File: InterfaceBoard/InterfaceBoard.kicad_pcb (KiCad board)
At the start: 4 copper layers, 100 x 86 mm, 137 parts, among them J1 Conn_ARM_JTAG_SWD_10, J2 USB_B, J3 Keithley_50-Pin_Connector, J4 DB9_Female_MountingHoles, P1 RB1-125BAG1A, Q1 BC848W, Q2 BC848W, Q3 BC848W, U1 W5500, U2 FT231XQ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

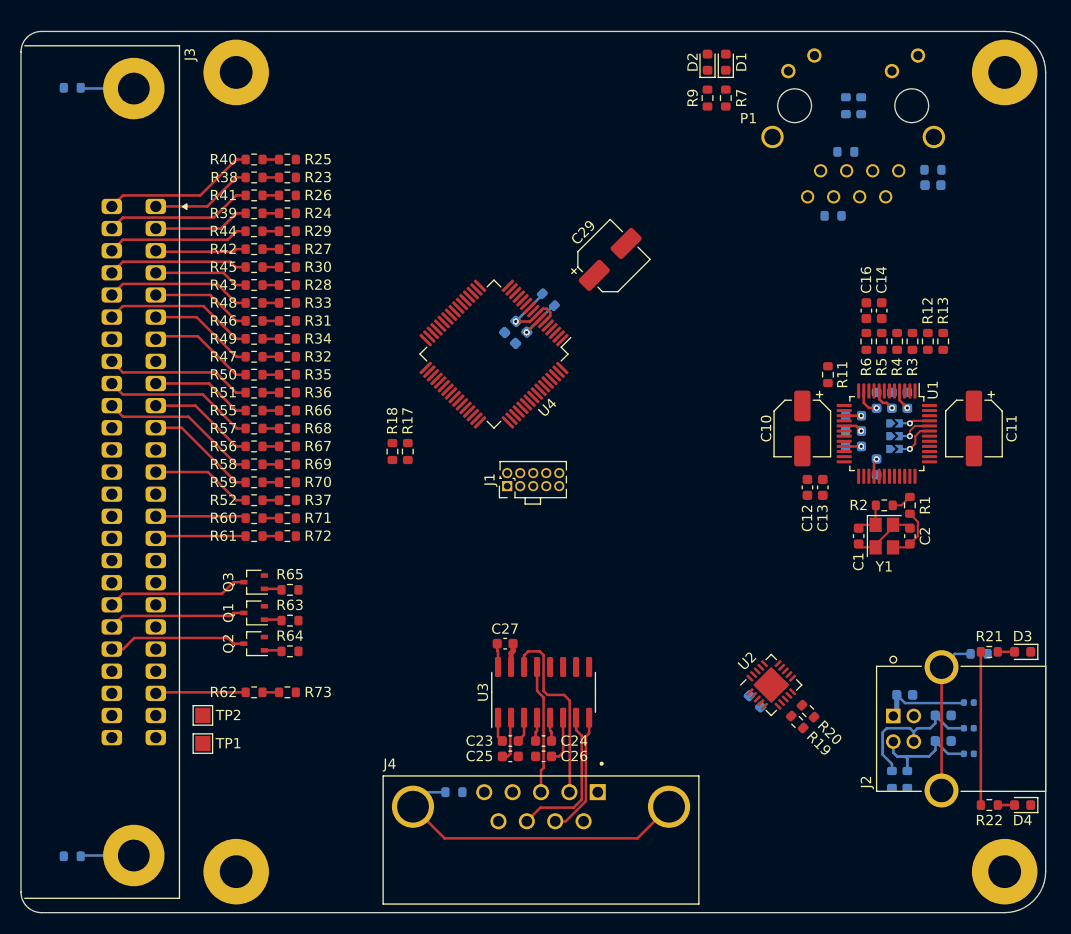
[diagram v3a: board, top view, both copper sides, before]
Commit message: InterfaceBoard: Update connector footprint
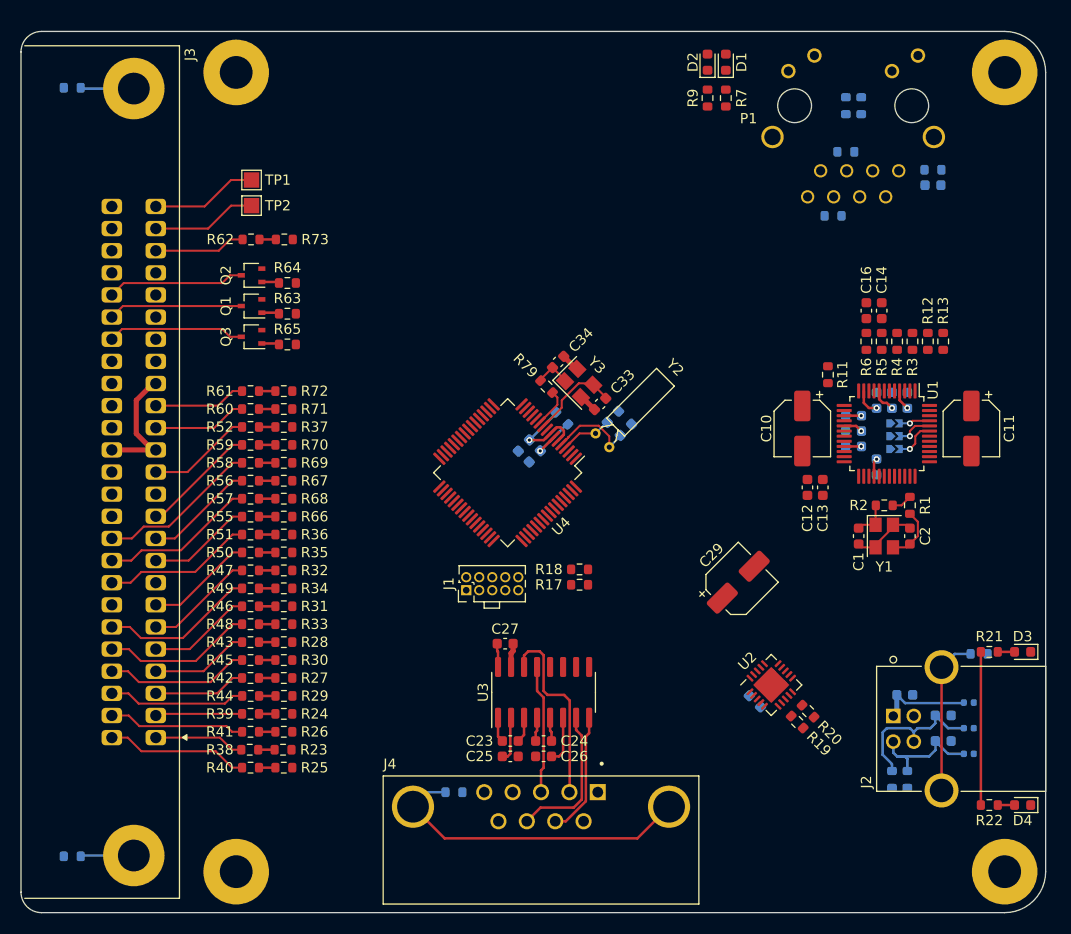
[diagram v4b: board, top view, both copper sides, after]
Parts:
- added C31: 22pF, Capacitor_SMD:C_0603_1608Metric, B.Cu at (97.8, 66.6)
- added C32: 22pF, Capacitor_SMD:C_0603_1608Metric, B.Cu at (99.0, 67.9)
- added C33: 12pF, Capacitor_SMD:C_0603_1608Metric, F.Cu at (96.5, 65.4)
- added C34: 12pF, Capacitor_SMD:C_0603_1608Metric, F.Cu at (92.4, 61.3)
- added R79: 1.6k, Resistor_SMD:R_0603_1608Metric, F.Cu at (91.3, 63.7)
- added Y2: 32.768 kHz, Crystal:Crystal_C26-LF_D2.1mm_L6.5mm_Horizontal, F.Cu at (97.4, 69.6)
- added Y3: 24 MHz, Crystal:Crystal_SMD_3225-4Pin_3.2x2.5mm, F.Cu at (94.5, 63.3)
- moved R25 59.4 mm to (65.7, 100.8)
- moved R40 59.4 mm to (62.4, 100.8)
- moved R23 55.9 mm to (65.6, 99.1)
- moved R38 55.9 mm to (62.3, 99.1)
- moved TP1 55.2 mm to (62.5, 43.5), turned to 90 degrees
- moved R26 52.4 mm to (65.7, 97.3)
- moved R41 52.4 mm to (62.4, 97.3)
- moved TP2 50.0 mm to (62.5, 46.0), turned to 90 degrees
- moved R24 48.9 mm to (65.7, 95.6)
- moved R39 48.9 mm to (62.4, 95.6)
- moved R29 45.4 mm to (65.7, 93.8)
- moved R44 45.4 mm to (62.4, 93.8)
- moved R62 44.2 mm to (62.5, 49.3)
- moved R73 44.2 mm to (65.7, 49.3)
- moved R27 41.9 mm to (65.7, 92.1)
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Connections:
- net /USB/USB_PULLUP renamed /MCU/USB_PULLUP
- J1 pad 1: unconnected-(J1-Pad1) -> +3V3
- U4 pad 10: unconnected-(U4-Pad10) -> Net-(C33-Pad1)
- U4 pad 11: unconnected-(U4-Pad11) -> Net-(R79-Pad2)
- U4 pad 13: unconnected-(U4-Pad13) -> /Print_Cmd
- U4 pad 14: unconnected-(U4-Pad14) -> /Trigger
- U4 pad 15: /Data_4e0 -> /Hold2
- U4 pad 16: /Data_1e0 -> /Hold1
- U4 pad 19: unconnected-(U4-Pad19) -> /Sensitivity_1e0
- U4 pad 22: unconnected-(U4-Pad22) -> /Polarity
- U4 pad 24: unconnected-(U4-Pad24) -> /Range_1e1
- U4 pad 25: /Data_8e0 -> /Range_8e0
- U4 pad 26: /Data_2e0 -> /Range_2e0
- U4 pad 27: /Data_4e1 -> /Range_4e0
- U4 pad 28: /Data_1e1 -> /Range_1e0
- U4 pad 29: /Data_8e1 -> /Overload
- U4 pad 3: unconnected-(U4-Pad3) -> /Sensitivity_2e0
- U4 pad 30: /Data_2e1 -> /Data_1e3
- U4 pad 31: /Data_4e2 -> /Data_2e2
- U4 pad 32: /Data_1e2 -> /Data_8e2
- U4 pad 33: /Data_8e2 -> /Data_1e2
- U4 pad 34: /Data_2e2 -> /Data_4e2
- U4 pad 35: /Data_1e3 -> /Data_2e1
- U4 pad 36: /Overload -> /Data_8e1
- U4 pad 37: /Range_1e0 -> /Data_1e1
- U4 pad 38: /Range_4e0 -> /Data_4e1
- U4 pad 39: /Range_2e0 -> /Data_2e0
- U4 pad 4: unconnected-(U4-Pad4) -> Net-(C31-Pad1)
- U4 pad 40: /Range_8e0 -> /Data_8e0
- U4 pad 41: /Range_1e1 -> /Data_1e0
- U4 pad 42: /Polarity -> /Data_4e0
- U4 pad 47: /Sensitivity_1e0 -> unconnected-(U4-Pad47)
- U4 pad 48: /Sensitivity_2e0 -> unconnected-(U4-Pad48)
- U4 pad 49: /Hold1 -> unconnected-(U4-Pad49)
- U4 pad 5: unconnected-(U4-Pad5) -> Net-(C32-Pad1)
- U4 pad 50: /Hold2 -> unconnected-(U4-Pad50)
- U4 pad 51: /Trigger -> unconnected-(U4-Pad51)
- U4 pad 52: /Print_Cmd -> unconnected-(U4-Pad52)
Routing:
- net +15V: track 0.00 -> 12.7 mm
- net /50pin/Ref_Hi: track 0.00 -> 10.4 mm
- net /50pin/Ref_Lo: track 0.00 -> 10.3 mm
- net Net-(C33-Pad1): track 0.00 -> 8.92 mm
- net Net-(C32-Pad1): track 0.00 -> 8.51 mm
- net Net-(C31-Pad1): track 0.00 -> 5.16 mm
- net Net-(R79-Pad2): track 0.00 -> 3.84 mm
- net GND: track 8.83 -> 12.5 mm
- net Net-(C34-Pad1): track 0.00 -> 3.59 mm
- net Net-(J3-Pad1): track 9.94 -> 8.83 mm
- net Net-(J3-Pad27): track 14.4 -> 13.4 mm
- net Net-(J3-Pad26): track 15.0 -> 13.9 mm
- net Net-(J3-Pad2): track 9.39 -> 8.49 mm

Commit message: InterfaceBoard: Add 3.3 V regulater, test points.
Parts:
- added C35: 10 uF, Capacitor_SMD:C_0805_2012Metric, F.Cu at (86.2, 41.5)
- added C36: 100 nF, Capacitor_SMD:C_0603_1608Metric, F.Cu at (91.8, 43.5)
- added C37: 10 uF, Capacitor_SMD:C_0805_2012Metric, F.Cu at (84.2, 41.5)
- added C38: 22 uF, Capacitor_SMD:C_0805_2012Metric, F.Cu at (86.2, 45.0)
- added C39: 22 uF, Capacitor_SMD:C_0805_2012Metric, F.Cu at (84.2, 45.0)
- added FB1: 1k, Inductor_SMD:L_0805_2012Metric, F.Cu at (118.5, 70.8)
- added J5: SPI, Connector_PinHeader_1.27mm:PinHeader_1x06_P1.27mm_Vertical, F.Cu at (109.5, 105.9)
- added J6: RS232, Connector_PinHeader_1.27mm:PinHeader_1x05_P1.27mm_Vertical, F.Cu at (98.5, 96.1)
- added J7: UART, Connector_PinHeader_1.27mm:PinHeader_1x05_P1.27mm_Vertical, F.Cu at (116.8, 107.2)
- added L1: 2.2 uH, Inductor_SMD:L_Taiyo-Yuden_NR-50xx, F.Cu at (90.2, 47.0)
- added R80: 0, Resistor_SMD:R_0603_1608Metric, F.Cu at (80.0, 31.2)
- added R81: 0, Resistor_SMD:R_0603_1608Metric, F.Cu at (80.0, 32.8)
- added R82: 0, Resistor_SMD:R_0603_1608Metric, F.Cu at (80.0, 34.2)
- added R83: 31.6k, Resistor_SMD:R_0603_1608Metric, F.Cu at (91.8, 42.0)
- added R84: 10k, Resistor_SMD:R_0603_1608Metric, F.Cu at (91.8, 40.5)
- added TP3: V_In, TestPoint:TestPoint_THTPad_1.5x1.5mm_Drill0.7mm, F.Cu at (88.0, 32.8)
- added TP4: V_Switch, TestPoint:TestPoint_THTPad_1.5x1.5mm_Drill0.7mm, F.Cu at (94.8, 47.0)
- added TP5: V_3.3, TestPoint:TestPoint_THTPad_1.5x1.5mm_Drill0.7mm, F.Cu at (98.5, 42.2)
- added TP6: V_EXT, TestPoint:TestPoint_THTPad_2.0x2.0mm_Drill1.0mm, F.Cu at (72.5, 32.0)
- added TP7: GND, TestPoint:TestPoint_THTPad_2.0x2.0mm_Drill1.0mm, F.Cu at (68.5, 32.0)
- added U5: AP62250Z6, Package_TO_SOT_SMD:SOT-563, F.Cu at (88.8, 43.0)
- C10, C11: footprint Capacitor_SMD:CP_Elec_5x5.9 -> Capacitor_SMD:C_0805_2012Metric
- J1: value Conn_ARM_JTAG_SWD_10 -> SWD
- moved C11 13.2 mm to (120.5, 72.8)
- moved C29 10.9 mm to (101.2, 76.2)
- moved R11 7.59 mm to (121.0, 55.2), turned to 90 degrees
- moved C12 7.57 mm to (117.7, 66.0), turned to 180 degrees
- moved C13 6.02 mm to (117.7, 67.5), turned to 180 degrees
- moved C10 4.19 mm to (117.5, 63.8), turned to 180 degrees
- moved C14 4.00 mm to (124.0, 52.2)
- moved C16 4.00 mm to (122.5, 52.2)
- moved R12 4.00 mm to (128.5, 55.2)
- moved R13 4.00 mm to (130.0, 55.2)
- moved R3 4.00 mm to (127.0, 55.2)
- moved R4 4.00 mm to (125.5, 55.3)
- moved R5 4.00 mm to (124.0, 55.2)
- moved R6 4.00 mm to (122.5, 55.2)
- moved C1 2.85 mm to (122.5, 75.5)
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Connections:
- net /USB/V_USB renamed /Power Supply/V_USB
- C10 pad 1: +3V3 -> /Ethernet Interface/W5500_AVDD
- C3 pad 2: +3V3 -> /Ethernet Interface/W5500_AVDD
- C4 pad 2: +3V3 -> /Ethernet Interface/W5500_AVDD
- C5 pad 2: +3V3 -> /Ethernet Interface/W5500_AVDD
- C6 pad 2: +3V3 -> /Ethernet Interface/W5500_AVDD
- C7 pad 2: +3V3 -> /Ethernet Interface/W5500_AVDD
- C9 pad 2: +3V3 -> /Ethernet Interface/W5500_AVDD
- U1 pad 11: +3V3 -> /Ethernet Interface/W5500_AVDD
- U1 pad 15: +3V3 -> /Ethernet Interface/W5500_AVDD
- U1 pad 17: +3V3 -> /Ethernet Interface/W5500_AVDD
- U1 pad 21: +3V3 -> /Ethernet Interface/W5500_AVDD
- U1 pad 4: +3V3 -> /Ethernet Interface/W5500_AVDD
- U1 pad 8: +3V3 -> /Ethernet Interface/W5500_AVDD
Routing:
- net /Ethernet Interface/W5500_AVDD: track 0.00 -> 26.6 mm, vias 0 -> 6
- net /Power Supply/V_IN: track 0.00 -> 8.17 mm
- net /Power Supply/SW_Inductor: track 0.00 -> 6.26 mm
- net Net-(R6-Pad1): track 0.00 -> 6.19 mm
- net Net-(R11-Pad1): track 0.00 -> 5.99 mm
- net /Ethernet Interface/ETH_PORT_TX+: track 0.00 -> 5.86 mm
- net Net-(R5-Pad1): track 0.00 -> 5.78 mm
- net Net-(R4-Pad1): track 0.00 -> 5.78 mm
- net Net-(R3-Pad1): track 0.00 -> 5.37 mm
- net Net-(R1-Pad2): track 2.02 -> 5.30 mm
- net Net-(R83-Pad2): track 0.00 -> 3.13 mm
- net Net-(C1-Pad2): track 3.69 -> 6.56 mm
- net +3V3: track 23.0 -> 25.2 mm, vias 8 -> 4
- net Net-(C13-Pad1): track 0.00 -> 1.92 mm
- net Net-(C12-Pad1): track 0.00 -> 1.92 mm
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- added copper zone on F.Cu, net +3V3
- added copper zone on F.Cu, net /Power Supply/SW_Inductor
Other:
- board text added: "+15V"
- board text added: "3.3 V Regulator"
- board text added: "3V3"
- board text added: "CS"
- board text added: "CTS"
- board text added: "EXT"
- board text added: "GND"
- board text added: "PICO"
- board text added: "POCI"
- board text added: "RTS"
- board text added: "RX"
- board text added: "SCK"
- board text added: "TX"
- board text added: "USB"

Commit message: InterfaceBoard: MAX232 -> MAX3232
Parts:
- C23, C24, C25, C26: value 1uF -> 100nF
- U3: value MAX232 -> MAX3232
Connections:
- C27 pad 1: +5V -> +3V3
- U3 pad 16: +5V -> +3V3
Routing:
- net +5V: track 2.31 -> 0.00 mm
- net +3V3: track 25.2 -> 27.5 mm

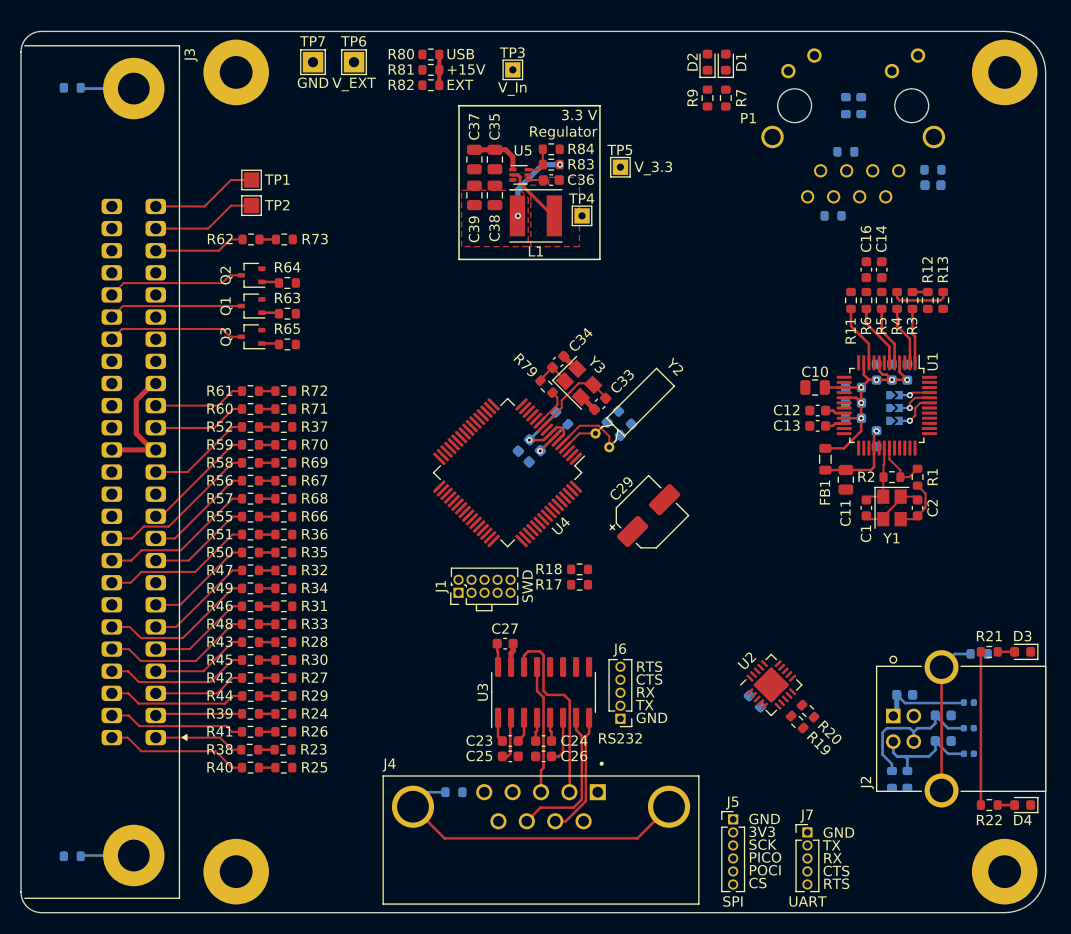
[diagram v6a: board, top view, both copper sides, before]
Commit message: InterfaceBoard: Routed Ethernet
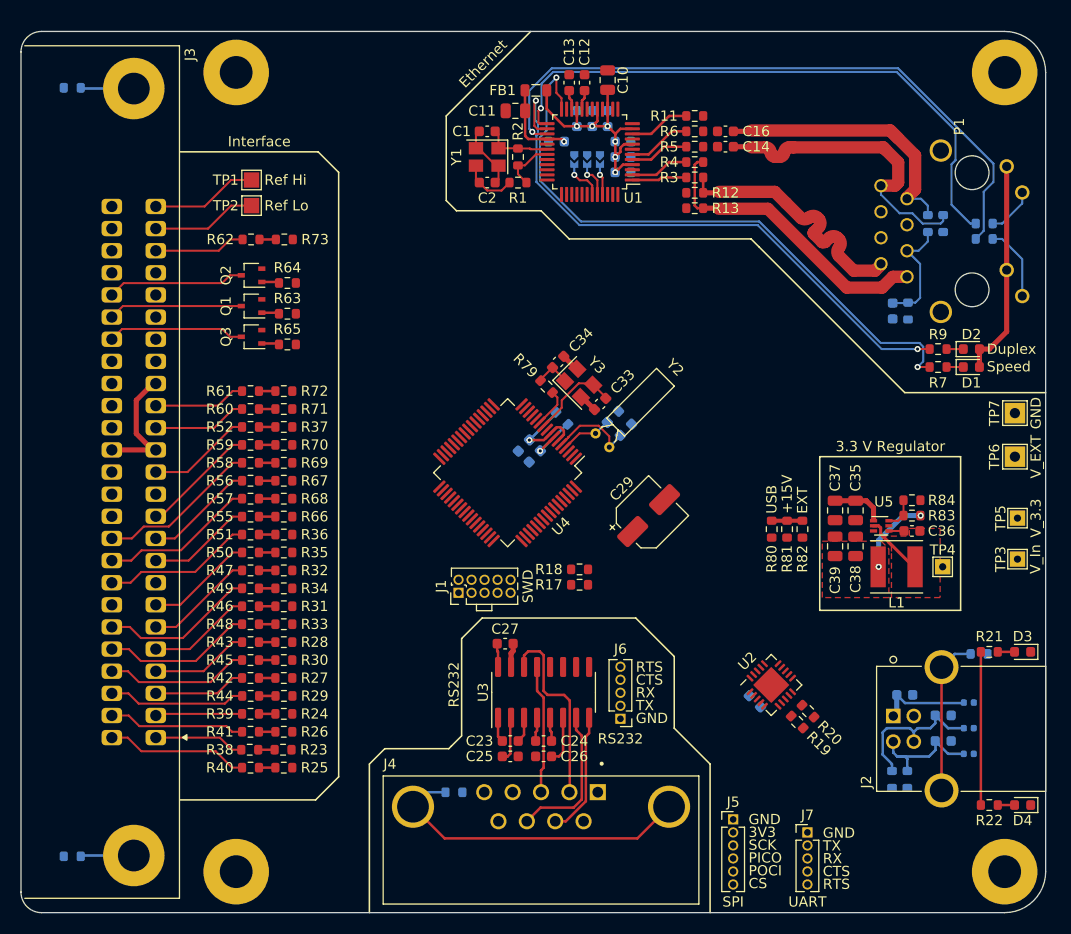
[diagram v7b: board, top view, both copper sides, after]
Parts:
- moved TP7 76.6 mm to (137.0, 66.2), turned to 90 degrees
- moved TP6 75.1 mm to (137.0, 70.5), turned to 90 degrees
- moved TP3 68.6 mm to (137.2, 80.5), turned to 90 degrees
- moved R80 57.0 mm to (113.3, 77.6), turned to 90 degrees
- moved R81 56.7 mm to (114.8, 77.6), turned to 90 degrees
- moved R82 56.5 mm to (116.3, 77.6), turned to 90 degrees
- moved C2 52.7 mm to (85.5, 43.8), turned to 180 degrees
- moved Y1 52.3 mm to (85.5, 41.2), turned to 180 degrees
- moved C1 52.1 mm to (85.5, 38.8), turned to 0 degrees
- moved TP5 51.7 mm to (137.2, 76.5), turned to 90 degrees
- moved C35 49.1 mm to (121.5, 75.8)
- moved C36 49.1 mm to (127.0, 77.8)
- moved C37 49.1 mm to (119.5, 75.8)
- moved C38 49.1 mm to (121.5, 79.2)
- moved C39 49.1 mm to (119.5, 79.2)
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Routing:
- net Net-(R10-Pad1): track 0.00 -> 63.8 mm, vias 0 -> 1
- net Net-(R7-Pad1): track 0.00 -> 61.5 mm, vias 0 -> 2
- net Net-(R8-Pad1): track 0.00 -> 58.6 mm, vias 0 -> 1
- net Net-(R9-Pad1): track 0.00 -> 57.2 mm, vias 0 -> 2
- net /Ethernet Interface/ETH_PORT_RX-: track 0.00 -> 30.6 mm
- net /Ethernet Interface/ETH_PORT_RX+: track 0.00 -> 27.6 mm
- net /Ethernet Interface/ETH_PORT_TX-: track 1.50 -> 25.7 mm
- net /Ethernet Interface/ETH_PORT_TX+: track 5.86 -> 29.4 mm
- net +3V3: track 27.5 -> 48.7 mm
- net /Ethernet Interface/ETH_PORT_CT: track 0.00 -> 11.4 mm
- net /Ethernet Interface/ETH_LED_ACT: track 0.00 -> 7.31 mm
- net /Ethernet Interface/ETH_LED_LINK: track 0.00 -> 4.77 mm
- net Net-(D1-Pad1): track 0.00 -> 1.64 mm
- net Net-(D2-Pad1): track 0.00 -> 1.64 mm
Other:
- board text added: "Ethernet"
- board text added: "Interface"
- board text added: "RS232"
- board text added: "Routed Ethernet differential pairs assuming 2-layer Redo if switching to 4-layer board"

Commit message: InterfaceBoard: Routed some digital interfaces to MCU
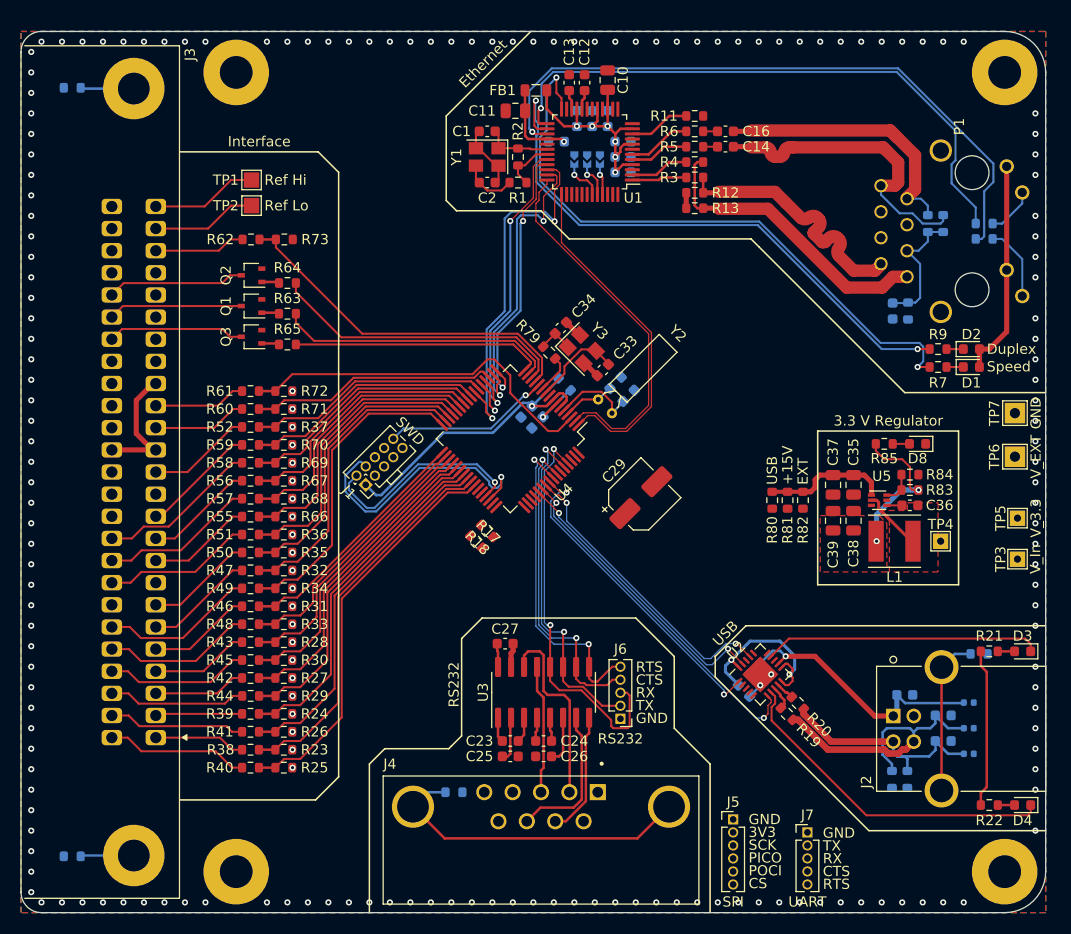
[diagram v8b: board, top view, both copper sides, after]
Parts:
- added D8: Red, LED_SMD:LED_0603_1608Metric, F.Cu at (127.5, 69.2)
- added R85: 1k, Resistor_SMD:R_0603_1608Metric, F.Cu at (124.2, 69.2)
- moved J1 13.9 mm to (73.6, 73.2), turned to 135 degrees
- moved R17 10.4 mm to (85.5, 77.8), turned to 135 degrees
- moved R18 10.4 mm to (84.4, 78.8), turned to 135 degrees
- moved R78 3.32 mm to (93.1, 63.4)
- moved C30 3.32 mm to (90.4, 67.2)
- moved C32 3.32 mm to (99.3, 64.6)
- moved C34 3.32 mm to (92.7, 57.9)
- moved R79 3.32 mm to (91.5, 60.3)
- moved U4 3.32 mm to (87.8, 68.8)
- moved Y3 3.32 mm to (94.7, 60.0)
- moved C28 3.32 mm to (89.3, 66.1)
- moved C31 3.32 mm to (98.0, 63.3)
- moved C33 3.32 mm to (96.8, 62.0)
- moved Y2 3.32 mm to (97.7, 66.3)
- moved R80 2.83 mm to (113.3, 74.8)
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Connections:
- U4 pad 1: unconnected-(U4-Pad1) -> /Ethernet Interface/Reset
- U4 pad 2: unconnected-(U4-Pad2) -> /Ethernet Interface/Int
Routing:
- net /MCU/RS232_RX: track 0.00 -> 39.6 mm, vias 0 -> 2
- net /Data_4e0: track 1.60 -> 39.3 mm
- net /Ethernet Interface/Int: track 0.00 -> 36.1 mm
- net /Data_1e0: track 1.60 -> 37.6 mm
- net /Ethernet Interface/POCI: track 0.00 -> 35.5 mm, vias 0 -> 2
- net /Sensitivity_2e0: track 1.60 -> 36.2 mm
- net /MCU/USB_UART_RTS: track 0.00 -> 34.6 mm, vias 0 -> 2
- net /Data_8e0: track 1.60 -> 35.9 mm
- net /MCU/RS232_TX: track 0.00 -> 33.8 mm, vias 0 -> 2
- net /Print_Cmd: track 1.60 -> 35.4 mm
- net /Ethernet Interface/Reset: track 0.00 -> 33.5 mm
- net /USB/FTDI_TX_LED: track 0.00 -> 33.1 mm
- net /Data_2e0: track 1.60 -> 34.2 mm
- net /MCU/RS232_RTS: track 0.00 -> 32.0 mm, vias 0 -> 2
- net /MCU/USB_UART_RX: track 0.00 -> 31.9 mm, vias 0 -> 2
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- added copper zone on B.Cu, net GND
- added copper zone on F.Cu, net GND
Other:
- copper layers 4 -> 2
- board text added: "TODO: Add chassis ground, and pour under RJ45 jack, but not under rx/tx pins."
